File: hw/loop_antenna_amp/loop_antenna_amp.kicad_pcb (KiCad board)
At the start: 2 copper layers, 88.9 x 78.7 mm, 77 parts, among them J1 ANT1, J2 ANT2, J3 GND, J4 Coax (SMA), Q1 MMBT3904, Q2 MMBT3904, Q3 MMBT3904, Q4 MMBT3904, Q5 PZT3904, Q6 PZT3904, T1 Isolation trafo, T2 Normalization trafo, T3 Output balun, U1 L78L10, U2 TL072

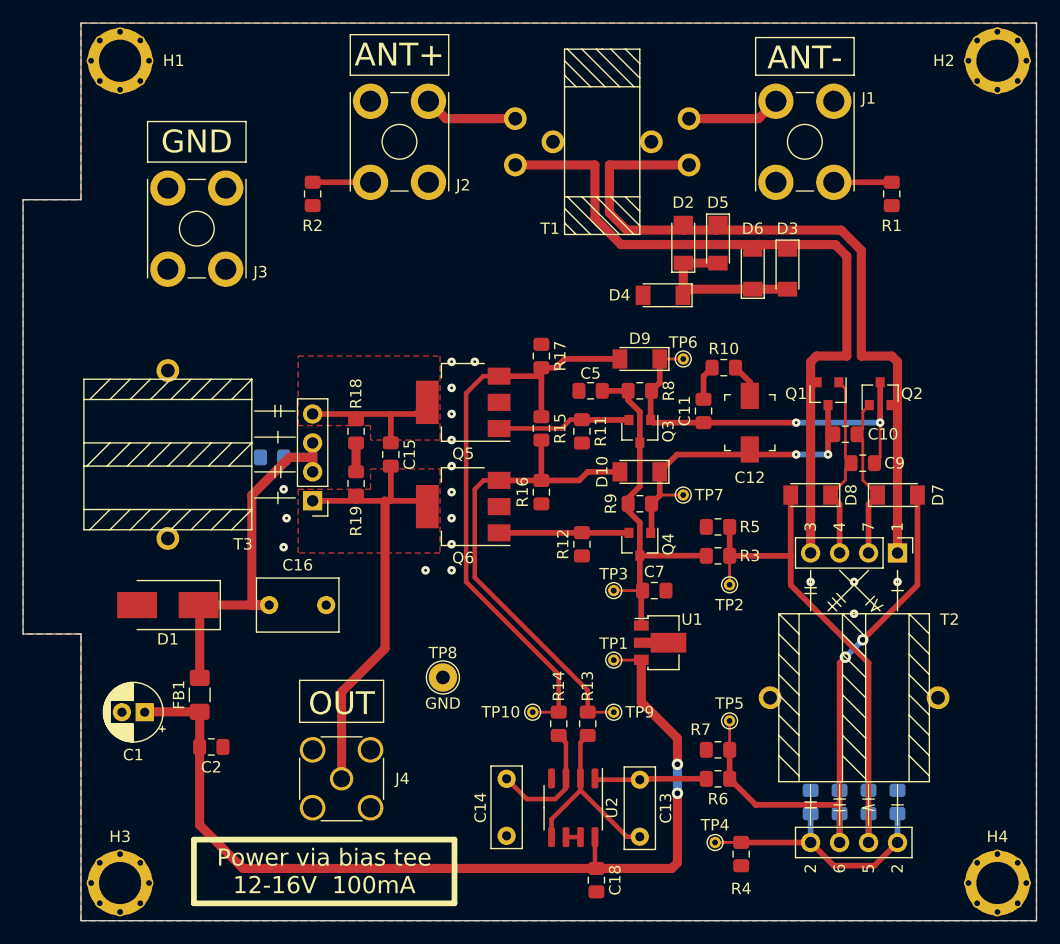
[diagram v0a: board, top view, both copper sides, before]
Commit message: Loop antenna: initial PCB layout completed
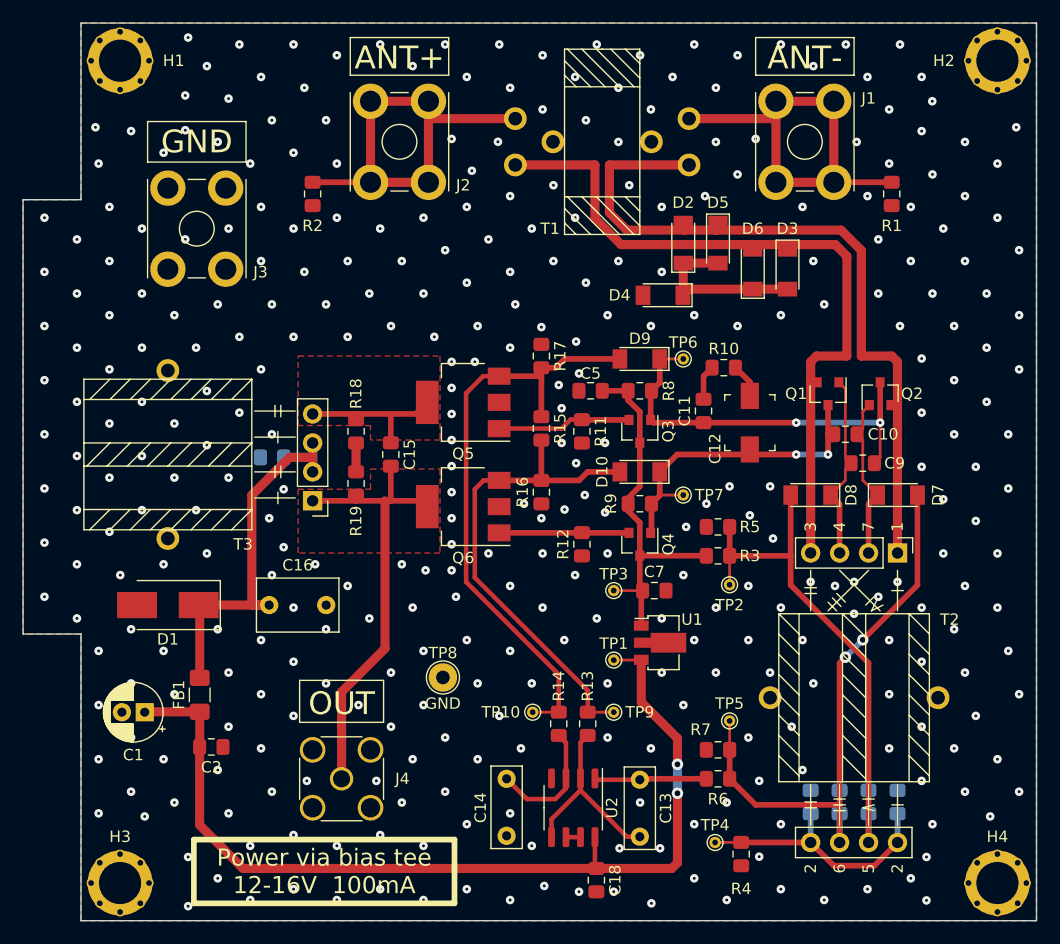
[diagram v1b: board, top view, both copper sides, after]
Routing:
- net Net-(J2-Pad1): track 13.3 -> 37.1 mm
- net Net-(J1-Pad1): track 13.3 -> 37.1 mm
- net GND: vias 18 -> 357
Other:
- board text added: "Loop antenna amplifier 0.1-30 MHz R.D. 2021"

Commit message: Loop antenna: make mounting holes more stable
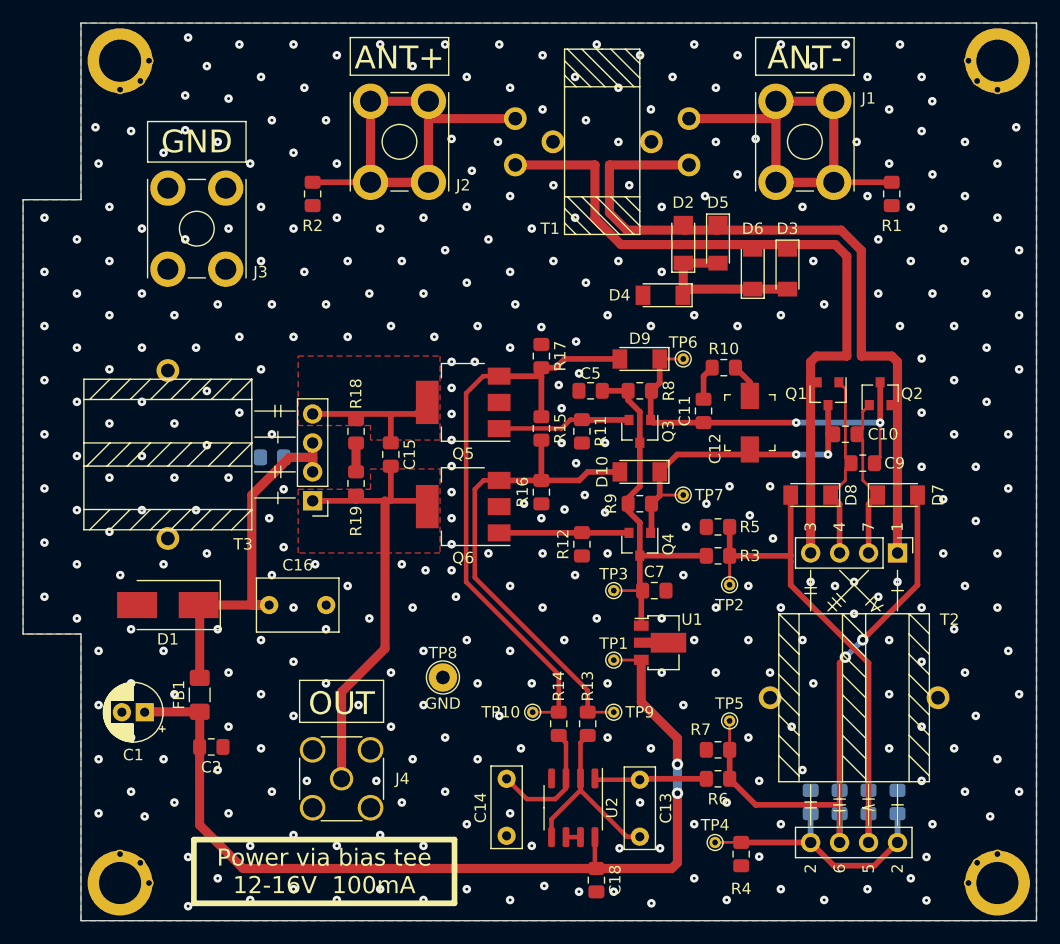
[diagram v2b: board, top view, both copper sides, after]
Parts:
- turned H2 to 270 degrees
- turned H3 to 90 degrees
- turned H4 to 180 degrees

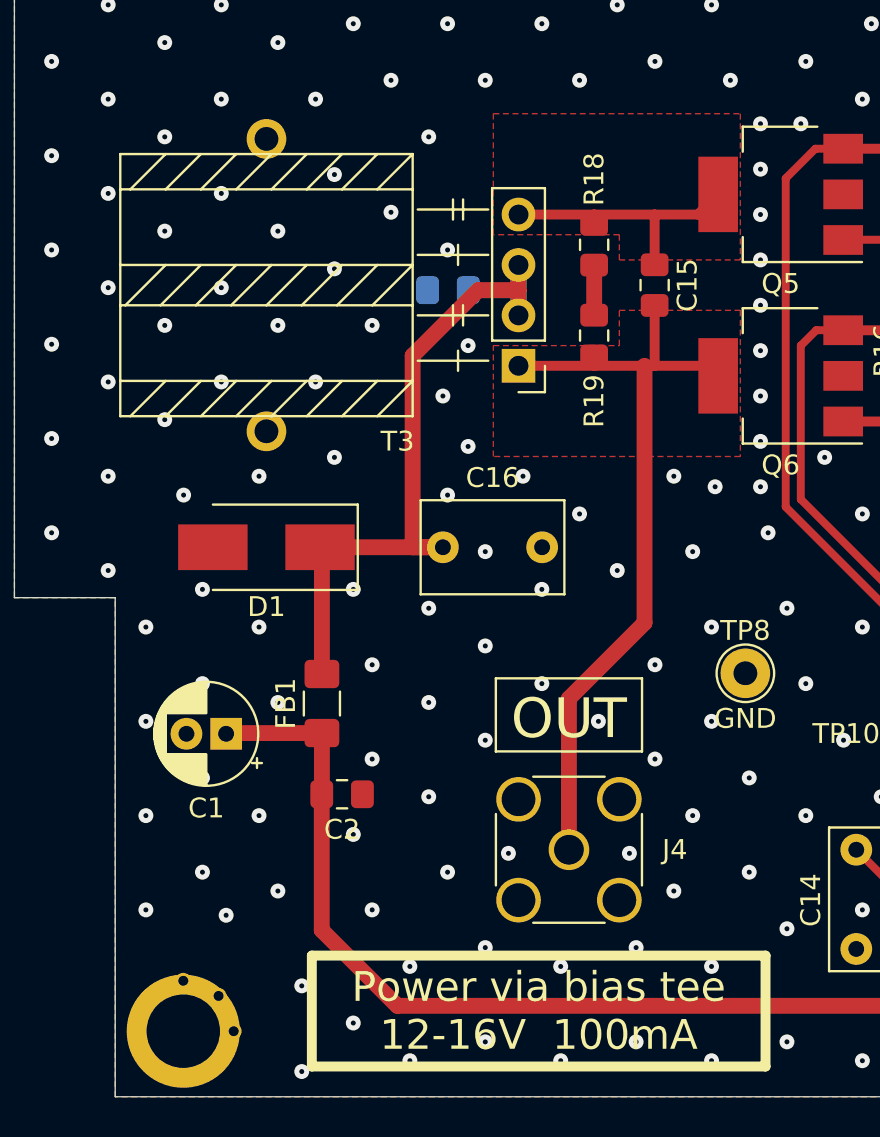
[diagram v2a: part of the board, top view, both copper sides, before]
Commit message: Loop antenna: fix balun footprint
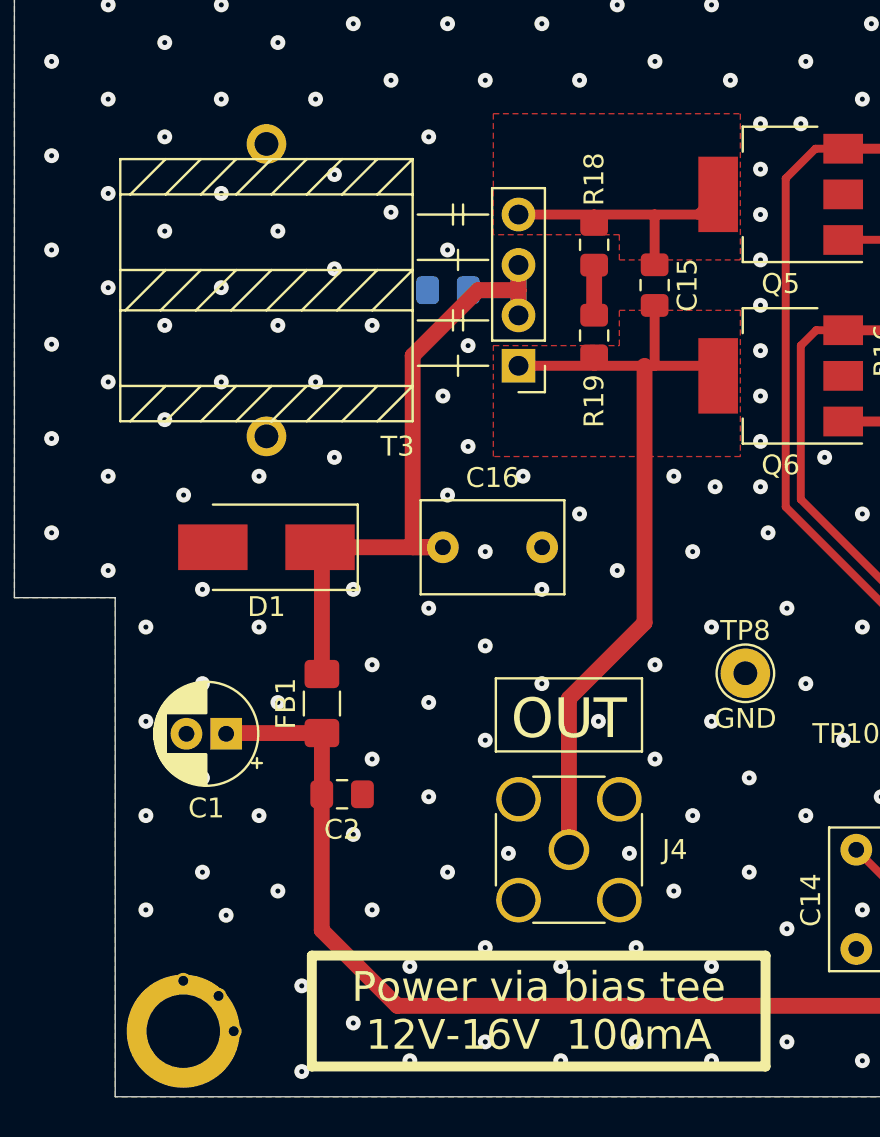
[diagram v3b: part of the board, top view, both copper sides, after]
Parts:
- moved T3 0.25 mm to (40.6, 91.2)
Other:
- board text added: "Power via bias tee 12V-16V 100mA"
- board text removed: "Power via bias tee 12-16V 100mA"

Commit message: Loop antenna: improve silkscreen
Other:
- board text added: "Mounting pattern: Gainta G113"
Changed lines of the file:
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@@
   (general
     (thickness 1.6)
-    (drawings 41)
+    (drawings 66)
     (tracks 622)
     (zones 0)
@@
     (tags "capacitor handsolder")
     (attr smd)
-    (fp_text reference C17 (at 0 1.65) (layer B.SilkS)
+    (fp_text reference C17 (at 0 -1.778) (layer B.SilkS)
       (effects (font (size 1 1) (thickness 0.15)) (justify mirror))
     )
@@
     (tags "capacitor handsolder")
     (attr smd)
-    (fp_text reference C6 (at 3.302 0 90) (layer B.SilkS)
+    (fp_text reference C6 (at 3.302 0.508 90) (layer B.SilkS)
       (effects (font (size 1 1) (thickness 0.15)) (justify mirror))
     )
@@
     )
   )
+  (gr_line (start 61.214 80.264) (end 61.214 81.534) (layer B.SilkS) (width 0.12))
+  (gr_line (start 58.166 80.264) (end 61.214 80.264) (layer B.SilkS) (width 0.12))
+  (gr_line (start 58.166 81.534) (end 58.166 80.264) (layer B.SilkS) (width 0.12))
+  (gr_line (start 56.642 81.534) (end 58.166 81.534) (layer B.SilkS) (width 0.12))
+  (gr_line (start 57.658 99.018782) (end 58.166 98.298) (layer B.SilkS) (width 0.12))
+  (gr_line (start 57.658 99.018782) (end 57.15 98.298) (layer B.SilkS) (width 0.12))
+  (gr_line (start 57.658 83.353218) (end 58.166 84.074) (layer B.SilkS) (width 0.12))
+  (gr_line (start 57.658 83.353218) (end 57.15 84.074) (layer B.SilkS) (width 0.12))
+  (gr_line (start 61.426782 82.55) (end 60.706 83.058) (layer B.SilkS) (width 0.12))
+  (gr_line (start 61.426782 82.55) (end 60.706 82.042) (layer B.SilkS) (width 0.12))
+  (gr_line (start 58.461218 82.55) (end 59.182 83.058) (layer B.SilkS) (width 0.12))
+  (gr_line (start 58.461218 82.55) (end 59.182 82.042) (layer B.SilkS) (width 0.12))
+  (gr_line (start 56.642 100.838) (end 56.642 81.534) (layer B.SilkS) (width 0.12))
+  (gr_line (start 63.246 100.838) (end 56.642 100.838) (layer B.SilkS) (width 0.12))
+  (gr_line (start 63.246 81.534) (end 63.246 100.838) (layer B.SilkS) (width 0.12))
+  (gr_line (start 61.214 81.534) (end 63.246 81.534) (layer B.SilkS) (width 0.12))
+  (gr_circle (center 62.23 82.55) (end 62.484 81.788) (layer B.SilkS) (width 0.12))
+  (gr_circle (center 57.658 82.55) (end 57.912 81.788) (layer B.SilkS) (width 0.12))
+  (gr_circle (center 57.658 99.822) (end 57.912 99.06) (layer B.SilkS) (width 0.12))
+  (gr_circle (center 62.23 99.822) (end 62.484 99.06) (layer B.SilkS) (width 0.12))
+  (gr_line (start 57.658 99.018782) (end 57.658 83.353218) (layer B.SilkS) (width 0.12))
+  (gr_line (start 61.426782 99.822) (end 58.461218 99.822) (layer B.SilkS) (width 0.12))
+  (gr_line (start 62.23 83.353218) (end 62.23 99.018782) (layer B.SilkS) (width 0.12))
+  (gr_line (start 58.461218 82.55) (end 61.426782 82.55) (layer B.SilkS) (width 0.12))
+  (gr_text "Mounting pattern:\nGainta G113" (at 59.944 91.186 90) (layer B.SilkS)
+    (effects (font (size 1 1) (thickness 0.15)) (justify mirror))
+  )
   (gr_line (start 74.676 93.218) (end 74.676 85.344) (layer B.SilkS) (width 0.12))

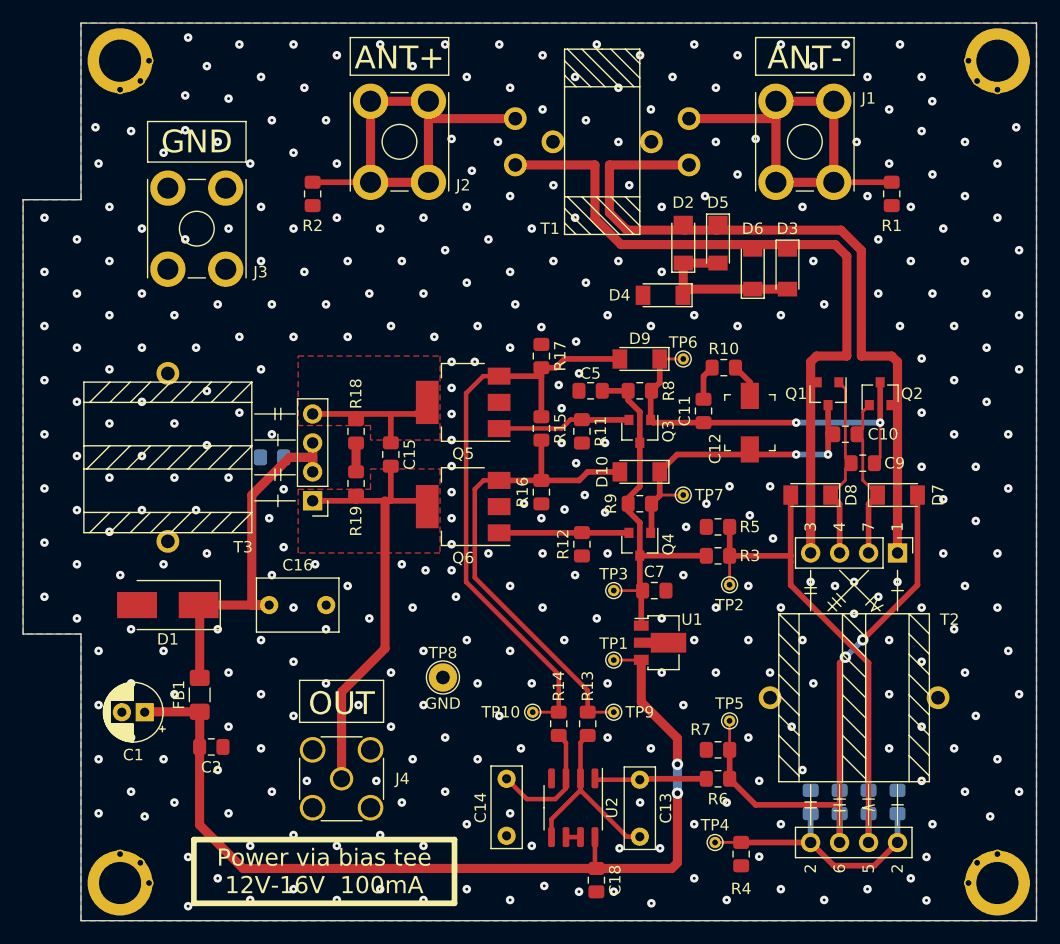
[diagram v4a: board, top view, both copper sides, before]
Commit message: Loop antenna amp: update PCB to match schematic
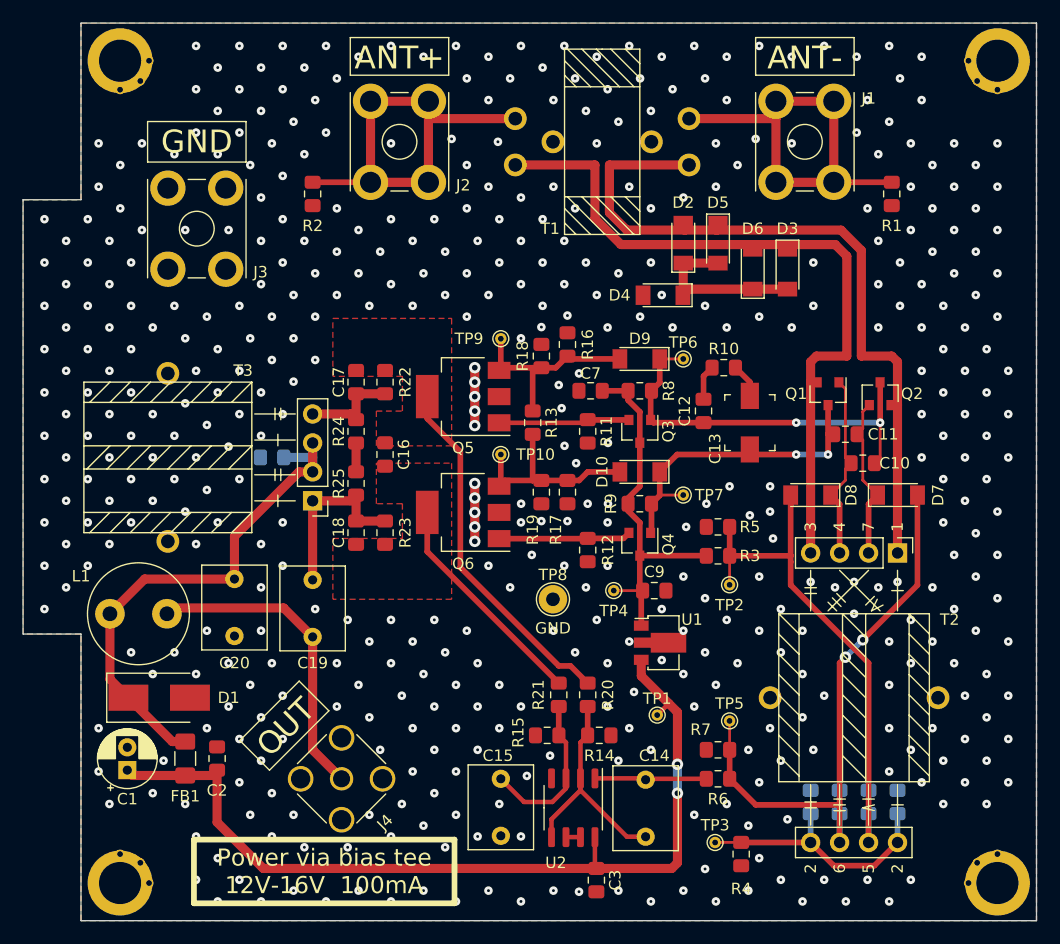
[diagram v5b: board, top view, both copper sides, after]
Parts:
- removed the C16 at (49.5, 104.1)
- added C17: 100n, Capacitor_SMD:C_0805_2012Metric_Pad1.15x1.40mm_HandSolder, F.Cu at (57.1, 84.6)
- added C18: 100n, Capacitor_SMD:C_0805_2012Metric_Pad1.15x1.40mm_HandSolder, F.Cu at (57.1, 97.8)
- added C19: 1u, Capacitor_THT:C_Rect_L7.2mm_W5.5mm_P5.00mm_FKS2_FKP2_MKS2_MKP2, F.Cu at (53.3, 106.9)
- added C20: 1u, Capacitor_THT:C_Rect_L7.2mm_W5.5mm_P5.00mm_FKS2_FKP2_MKS2_MKP2, F.Cu at (46.5, 101.9)
- added L1: 1mH, Inductor_THT:L_Radial_D8.7mm_P5.00mm_Fastron_07HCP, F.Cu at (35.6, 104.9)
- added R13: 10, Resistor_SMD:R_0805_2012Metric_Pad1.15x1.40mm_HandSolder, F.Cu at (72.6, 88.1)
- added R16: DNP, Resistor_SMD:R_0805_2012Metric_Pad1.15x1.40mm_HandSolder, F.Cu at (75.7, 81.3)
- added R17: DNP, Resistor_SMD:R_0805_2012Metric_Pad1.15x1.40mm_HandSolder, F.Cu at (75.7, 94.2)
- added R21: 10k, Resistor_SMD:R_0805_2012Metric_Pad1.15x1.40mm_HandSolder, F.Cu at (74.9, 112.0)
- added R22: 10, Resistor_SMD:R_0805_2012Metric_Pad1.15x1.40mm_HandSolder, F.Cu at (59.7, 84.6)
- added R23: 10, Resistor_SMD:R_0805_2012Metric_Pad1.15x1.40mm_HandSolder, F.Cu at (59.7, 97.8)
- C14: renamed from C13; value 100n -> 1u; footprint Capacitor_THT:C_Rect_L7.0mm_W2.5mm_P5.00mm -> Capacitor_THT:C_Rect_L7.2mm_W5.5mm_P5.00mm_FKS2_FKP2_MKS2_MKP2
- C15: renamed from C14; value 100n -> 1u; footprint Capacitor_THT:C_Rect_L7.0mm_W2.5mm_P5.00mm -> Capacitor_THT:C_Rect_L7.2mm_W5.5mm_P5.00mm_FKS2_FKP2_MKS2_MKP2
- R15: value 10 -> 10k
- moved TP9 32.9 mm to (69.8, 80.8)
- moved R15 26.9 mm to (73.9, 115.6), turned to 180 degrees
- moved TP10 24.7 mm to (69.8, 90.9)
- moved TP8 11.8 mm to (74.4, 103.6)
- moved D1 8.16 mm to (39.9, 112.3), turned to 0 degrees
- moved TP1 6.15 mm to (83.6, 113.8)
- moved FB1 5.73 mm to (42.2, 117.6)
- moved C1 5.30 mm to (37.1, 118.6), turned to 90 degrees
- moved R14 3.70 mm to (78.5, 115.6), turned to 0 degrees
- moved R20 2.54 mm to (77.5, 112.0), turned to 270 degrees
- moved C2 1.14 mm to (45.0, 117.6), turned to 90 degrees
- moved R12 0.72 mm to (77.5, 99.3)
- moved C15 0.51 mm to (69.8, 119.4)
- moved C16 0.51 mm to (59.7, 90.9)
- moved C14 0.51 mm to (82.5, 124.5)
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- renumbered C9 to C10, C10 to C11, C11 to C12, C12 to C13, C15 to C16, C17 to C21, C18 to C3, C3 to C4, C4 to C5, C5 to C7, C7 to C9, R17 to R18, R16 to R19, R13 to R20, R18 to R24, R19 to R25, TP9 to TP10, TP4 to TP3, TP3 to TP4, TP10 to TP9
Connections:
- C14 pad 1: Net-(C13-Pad1) (its old number) -> Net-(C14-Pad1)
- C15 pad 1: Net-(C14-Pad1) -> Net-(C15-Pad1)
- C16 pad 1: Net-(C15-Pad1) -> Net-(C16-Pad1)
- C16 pad 2: Net-(C15-Pad2) -> Net-(C16-Pad2)
- J4 pad 1: Net-(C15-Pad2) -> Net-(C19-Pad1)
- Q5 pad 2: Net-(C15-Pad1) -> Net-(C16-Pad1)
- Q6 pad 2: Net-(C15-Pad2) -> Net-(C16-Pad2)
- R14 pad 2: Net-(D9-Pad2) -> GND
- R15 pad 1: Net-(D9-Pad2) -> Net-(C15-Pad1)
- R15 pad 2: Net-(D10-Pad2) -> GND
- R18 pad 1: GND -> Net-(D9-Pad2)
- R18 pad 2: Net-(D9-Pad2) -> GND
- R20 pad 1: Net-(C13-Pad1) (its old number) -> Net-(C16-Pad1)
- R20 pad 2: Net-(D10-Pad2) -> Net-(C14-Pad1)
- R24 pad 1: Net-(C15-Pad1) -> Net-(C17-Pad1)
- R25 pad 2: Net-(C15-Pad2) -> Net-(C18-Pad1)
- T3 pad 1: Net-(C15-Pad2) -> Net-(C18-Pad1)
- T3 pad 3: Net-(C15-Pad1) -> Net-(C17-Pad1)
- U2 pad 2: Net-(C13-Pad1) (its old number) -> Net-(C14-Pad1)
- U2 pad 3: Net-(C14-Pad1) -> Net-(C15-Pad1)
- U2 pad 5: Net-(C13-Pad1) (its old number) -> Net-(C14-Pad1)
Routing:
- net Net-(C15-Pad2): track 39.8 -> 0.00 mm
- net Net-(D9-Pad2): track 52.4 -> 17.9 mm
- net Net-(C16-Pad1): track 0.00 -> 31.6 mm
- net Net-(C19-Pad1): track 0.00 -> 27.5 mm
- net Net-(D10-Pad2): track 42.8 -> 18.0 mm
- net Net-(C16-Pad2): track 0.00 -> 19.8 mm
- net Net-(C13-Pad1) (its old number): track 17.1 -> 0.00 mm
- net Net-(C18-Pad1): track 0.00 -> 15.8 mm
- net GND: track 0.00 -> 10.2 mm, vias 357 -> 483
- net /VFEED: track 38.1 -> 47.4 mm
- net Net-(C14-Pad1): track 11.2 -> 20.2 mm
- net Net-(C17-Pad1): track 0.00 -> 8.82 mm
- net VCC: track 82.8 -> 78.5 mm
- net Net-(C15-Pad1): track 13.5 -> 14.5 mm
- added copper zone on F.Cu, net Net-(C16-Pad1)
- added copper zone on F.Cu, net Net-(C16-Pad2)
- removed copper zone on F.Cu, net Net-(C15-Pad1)
- removed copper zone on F.Cu, net Net-(C15-Pad2)
